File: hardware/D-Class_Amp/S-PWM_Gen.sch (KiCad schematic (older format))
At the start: 15 parts, among them U301 TL972, U302 LMV393

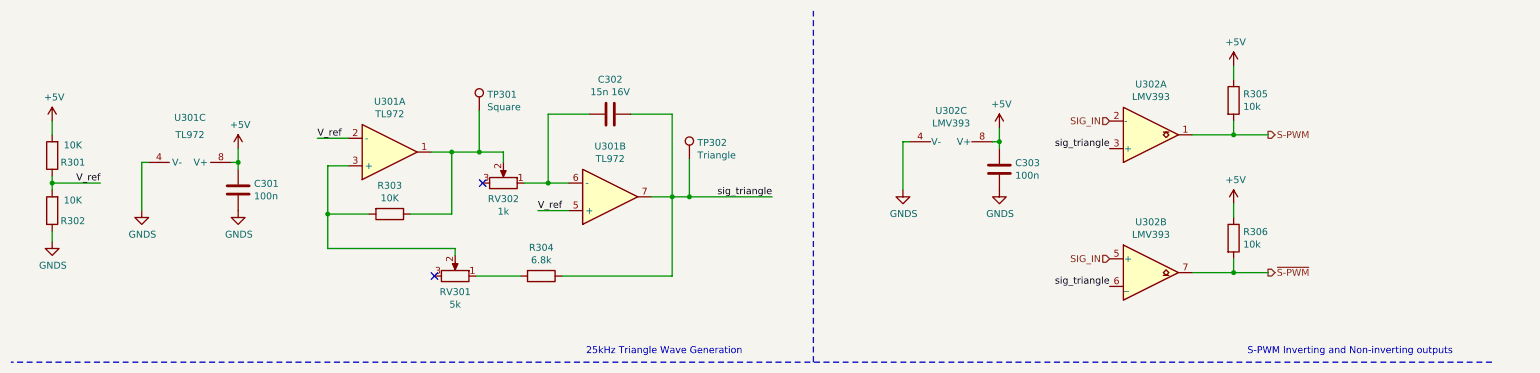
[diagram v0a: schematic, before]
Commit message: Add footprints to the output filter and select output filter components
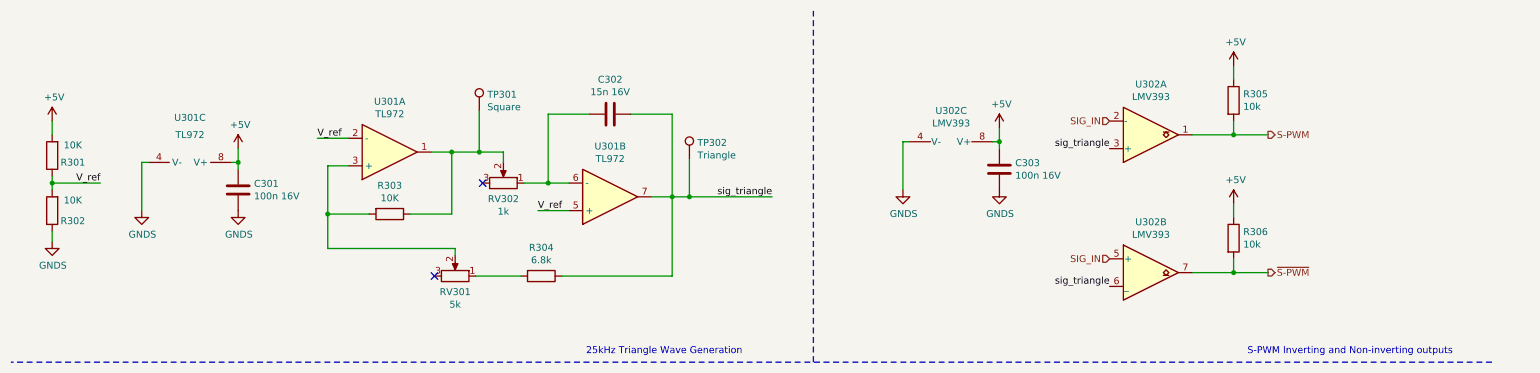
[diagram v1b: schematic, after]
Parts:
- C301, C303: value 100n -> 100n 16V
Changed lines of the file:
@@
 P 2125 1775
 F 0 "C301" H 2240 1821 50  0000 L CNN
-F 1 "100n" H 2240 1730 50  0000 L CNN
+F 1 "100n 16V" H 2240 1730 50  0000 L CNN
 F 2 "Resistor_SMD:R_0805_2012Metric_Pad1.20x1.40mm_HandSolder" H 2163 1625 50  0001 C CNN
 F 3 "~" H 2125 1775 50  0001 C CNN
@@
 P 7650 1625
 F 0 "C303" H 7765 1671 50  0000 L CNN
-F 1 "100n" H 7765 1580 50  0000 L CNN
+F 1 "100n 16V" H 7765 1580 50  0000 L CNN
 F 2 "Resistor_SMD:R_0805_2012Metric_Pad1.20x1.40mm_HandSolder" H 7688 1475 50  0001 C CNN
 F 3 "~" H 7650 1625 50  0001 C CNN

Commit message: added pricing and and part numbers to all components
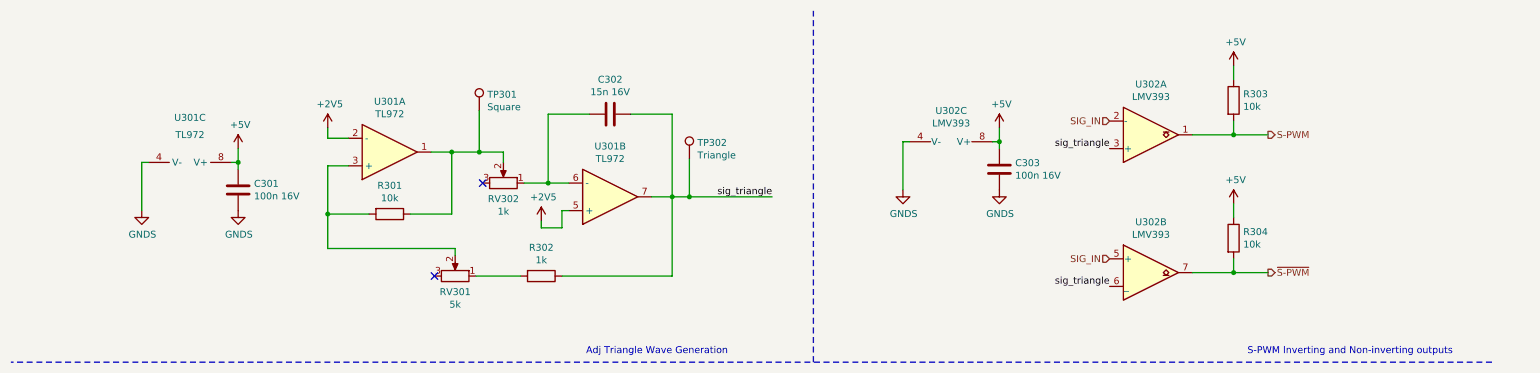
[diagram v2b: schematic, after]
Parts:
- removed R301, R302: 10K, Resistor_SMD:R_0805_2012Metric_Pad1.20x1.40mm_HandSolder, symbol Device:R
- C301, C303: footprint Resistor_SMD:R_0805_2012Metric_Pad1.20x1.40mm_HandSolder -> Capacitor_SMD:C_0805_2012Metric_Pad1.18x1.45mm_HandSolder; DigiKey Price (none) -> 0.16; Part Number (none) -> 885012207045
- C302: DigiKey Price (none) -> 0.16; Part Number (none) -> 885012207040
- R301: renamed from R303; value 10K -> 10k; DigiKey Price (none) -> 0.16; Part Number (none) -> RC0805JR-0710KL
- R302: renamed from R304; value 6.8k -> 1k; DigiKey Price (none) -> 0.16; Part Number (none) -> RC0805JR-0710KL
- R303: renamed from R305; DigiKey Price (none) -> 0.16; Part Number (none) -> RC0805JR-0710KL
- R304: renamed from R306; DigiKey Price (none) -> 0.16; Part Number (none) -> RC0805JR-0710KL
- RV301, RV302: DigiKey Price (none) -> 1.25
- U302: footprint Package_SO:VSSOP-8_3.0x3.0mm_P0.65mm -> Package_SO:SOIC-8_3.9x4.9mm_P1.27mm; DigiKey Price (none) -> 0.75; Part Number LMV393MMX -> LMV393S-13
- U302: footprint Package_SO:VSSOP-8_3.0x3.0mm_P0.65mm -> Package_SO:SOIC-8_3.9x4.9mm_P1.27mm; DigiKey Price (none) -> 0.75; Part Number (none) -> LMV393S-13
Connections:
- net V_ref renamed +2V5
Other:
- note added: "Adj Triangle Wave Generation"
- note removed: "25kHz Triangle Wave Generation"

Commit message: updated the BOM
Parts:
- TP301, TP302: footprint (none) -> TestPoint:TestPoint_THTPad_D2.0mm_Drill1.0mm
- U301: DigiKey Price (none) -> 1.47; Part Number (none) -> TL972IDR
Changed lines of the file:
@@
 F 2 "Package_SO:SOIC-8_3.9x4.9mm_P1.27mm" H 3225 1500 50  0001 C CNN
 F 3 "https://www.ti.com/lit/ds/symlink/tl971.pdf?HQS=dis-dk-null-digikeymode-dsf-pf-null-wwe&ts=1628641427496&ref_url=https%253A%252F%252Fwww.digikey.co.nz%252F" H 3225 1500 50  0001 C CNN
+F 4 "1.47" H 3225 1500 50  0001 C CNN "DigiKey Price"
+F 5 "TL972IDR" H 3225 1500 50  0001 C CNN "Part Number"
 	1    3225 1500
 	1    0    0    1
@@
 F 2 "Package_SO:SOIC-8_3.9x4.9mm_P1.27mm" H 4825 1825 50  0001 C CNN
 F 3 "https://www.ti.com/lit/ds/symlink/tl971.pdf?HQS=dis-dk-null-digikeymode-dsf-pf-null-wwe&ts=1628641427496&ref_url=https%253A%252F%252Fwww.digikey.co.nz%252F" H 4825 1825 50  0001 C CNN
+F 4 "1.47" H 4825 1825 50  0001 C CNN "DigiKey Price"
+F 5 "TL972IDR" H 4825 1825 50  0001 C CNN "Part Number"
 	2    4825 1825
 	1    0    0    1
@@
 F 2 "Package_SO:SOIC-8_3.9x4.9mm_P1.27mm" H 1775 1675 50  0001 C CNN
 F 3 "https://www.ti.com/lit/ds/symlink/tl971.pdf?HQS=dis-dk-null-digikeymode-dsf-pf-null-wwe&ts=1628641427496&ref_url=https%253A%252F%252Fwww.digikey.co.nz%252F" H 1775 1675 50  0001 C CNN
+F 4 "1.47" H 1775 1675 50  0001 C CNN "DigiKey Price"
+F 5 "TL972IDR" H 1775 1675 50  0001 C CNN "Part Number"
 	3    1775 1675
 	0    1    1    0
@@
 F 0 "TP302" H 5458 1668 50  0000 L CNN
 F 1 "Triangle" H 5458 1577 50  0000 L CNN
-F 2 "" H 5600 1550 50  0001 C CNN
+F 2 "TestPoint:TestPoint_THTPad_D2.0mm_Drill1.0mm" H 5600 1550 50  0001 C CNN
 F 3 "~" H 5600 1550 50  0001 C CNN
 	1    5400 1550
@@
 F 0 "TP301" H 3933 1318 50  0000 L CNN
 F 1 "Square" H 3933 1227 50  0000 L CNN
-F 2 "" H 4075 1200 50  0001 C CNN
+F 2 "TestPoint:TestPoint_THTPad_D2.0mm_Drill1.0mm" H 4075 1200 50  0001 C CNN
 F 3 "~" H 4075 1200 50  0001 C CNN
 	1    3875 1200

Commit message: placed and routed all components, fixed the MOSFET footprints, and added all 3D models.
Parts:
- TP301, TP302: footprint TestPoint:TestPoint_THTPad_D2.0mm_Drill1.0mm -> TestPoint:TestPoint_THTPad_D1.0mm_Drill0.5mm
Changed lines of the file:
@@
 F 0 "TP302" H 5458 1668 50  0000 L CNN
 F 1 "Triangle" H 5458 1577 50  0000 L CNN
-F 2 "TestPoint:TestPoint_THTPad_D2.0mm_Drill1.0mm" H 5600 1550 50  0001 C CNN
+F 2 "TestPoint:TestPoint_THTPad_D1.0mm_Drill0.5mm" H 5600 1550 50  0001 C CNN
 F 3 "~" H 5600 1550 50  0001 C CNN
 	1    5400 1550
@@
 F 0 "TP301" H 3933 1318 50  0000 L CNN
 F 1 "Square" H 3933 1227 50  0000 L CNN
-F 2 "TestPoint:TestPoint_THTPad_D2.0mm_Drill1.0mm" H 4075 1200 50  0001 C CNN
+F 2 "TestPoint:TestPoint_THTPad_D1.0mm_Drill0.5mm" H 4075 1200 50  0001 C CNN
 F 3 "~" H 4075 1200 50  0001 C CNN
 	1    3875 1200

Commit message: update design
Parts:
- R303, R304: value 10k -> 1k
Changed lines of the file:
@@
 P 9350 2125
 F 0 "R304" H 9420 2171 50  0000 L CNN
-F 1 "10k" H 9420 2080 50  0000 L CNN
+F 1 "1k" H 9420 2080 50  0000 L CNN
 F 2 "Resistor_SMD:R_0805_2012Metric_Pad1.20x1.40mm_HandSolder" V 9280 2125 50  0001 C CNN
 F 3 "~" H 9350 2125 50  0001 C CNN
@@
 P 9350 1125
 F 0 "R303" H 9420 1171 50  0000 L CNN
-F 1 "10k" H 9420 1080 50  0000 L CNN
+F 1 "1k" H 9420 1080 50  0000 L CNN
 F 2 "Resistor_SMD:R_0805_2012Metric_Pad1.20x1.40mm_HandSolder" V 9280 1125 50  0001 C CNN
 F 3 "~" H 9350 1125 50  0001 C CNN

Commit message: readded art and regen bom
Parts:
- RV301, RV302: symbol Device:R_POT -> D-Class_Amp-rescue:R_POT-Device
- U301: symbol Device:Opamp_Dual_Generic -> D-Class_Amp-rescue:Opamp_Dual_Generic-Device
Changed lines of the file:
@@
 $EndDescr
 $Comp
-L Device:Opamp_Dual_Generic U301
+L D-Class_Amp-rescue:Opamp_Dual_Generic-Device U301
 U 1 1 6104BA3C
 P 3225 1500
@@
 $EndComp
 $Comp
-L Device:Opamp_Dual_Generic U301
+L D-Class_Amp-rescue:Opamp_Dual_Generic-Device U301
 U 2 1 6104BF37
 P 4825 1825
@@
 $EndComp
 $Comp
-L Device:Opamp_Dual_Generic U301
+L D-Class_Amp-rescue:Opamp_Dual_Generic-Device U301
 U 3 1 6104C970
 P 1775 1675
@@
 S-PWM
 $Comp
-L Device:R_POT RV301
+L D-Class_Amp-rescue:R_POT-Device RV301
 U 1 1 6114E136
 P 3700 2400
@@
 NoConn ~ 3550 2400
 $Comp
-L Device:R_POT RV302
+L D-Class_Amp-rescue:R_POT-Device RV302
 U 1 1 611660D9
 P 4050 1725

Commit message: update pcb and simulations of sampling
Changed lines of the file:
@@
 Text Notes 4650 2975 0    50   ~ 0
 Adj Triangle Wave Generation
-Text Notes 9450 2975 0    50   ~ 0
+Text Notes 8225 2975 0    50   ~ 0
 S-PWM Inverting and Non-inverting outputs
 Wire Wire Line
